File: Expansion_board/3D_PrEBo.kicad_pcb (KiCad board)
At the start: 2 copper layers, 100 x 84 mm, 72 parts, among them J1 LED, J10 TMC_INPUT, J11 Power_out, J12 Z_Probe, J13 Fan_interconnection_header, J14 X_MIN, J15 Z_MAX, J2 V_IN, J3 RJ45, J4 X, J5 Y, J6 Z, J7 E0, J8 E1, J9 FAN&LED_INPUT, M1 Fan_3pin, M2 Fan_3pin, M3 Fan_3pin, M4 Fan_3pin, M5 Fan_3pin, M6 Fan_3pin, M7 Fan_3pin, M8 Fan_4pin, Q1 AOD4189, Q10 IRLML2502, Q2 IRLML2502, Q3 IRLML2502, Q4 IRLML2502, Q5 IRLML2502, Q6 IRLML2502, Q7 IRLML2502, Q8 IRLML2502, Q9 IRLML2502, U1 L5973D, U2 NCP1117-5.0_SOT223

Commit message: Expansion_board: PCB: Place all parts, routing of voltage regulator
Change horizontal fan connector to vertical.
Pour cooper planes on both sides.
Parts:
- C10, C11, C12, C13, C14, C7, C8, C9, JP1, JP2, Q10, Q2, Q3, Q4, Q5, Q6, Q7, Q8, Q9, R10, R11, R12, R13, R2, R6, R7, R8, R9: moved to B.Cu
- J1: footprint Connector_JST:JST_XH_S02B-XH-A-1_1x02_P2.50mm_Horizontal -> Connector_JST:JST_XH_B02B-XH-A_1x02_P2.50mm_Vertical
- J12: footprint Connector:FanPinHeader_1x04_P2.54mm_Vertical -> Connector_JST:JST_XH_B04B-XH-A_1x04_P2.50mm_Vertical
- M1, M2, M3, M4, M5, M6, M7: footprint Connector:FanPinHeader_1x03_P2.54mm_Vertical -> Connector_JST:JST_XH_S03B-XH-A_1x03_P2.50mm_Horizontal
- M8: footprint Connector:FanPinHeader_1x04_P2.54mm_Vertical -> Connector_JST:JST_XH_S04B-XH-A_1x04_P2.50mm_Horizontal
- moved Q3 301.3 mm to (108.6, 85.7), turned to 90 degrees
- moved R6 291.2 mm to (108.6, 89.5), turned to 180 degrees
- moved C1 288.6 mm to (131.6, 113.4)
- moved RV1 284.3 mm to (137.2, 116.8), turned to 180 degrees
- moved C8 283.1 mm to (111.0, 66.0), turned to 180 degrees
- moved D4 273.9 mm to (116.8, 113.8), turned to 180 degrees
- moved C9 273.3 mm to (123.7, 66.0), turned to 180 degrees
- moved R7 272.0 mm to (121.9, 89.5), turned to 180 degrees
- moved M2 271.9 mm to (127.0, 68.6), turned to 180 degrees
- moved Q1 270.2 mm to (127.5, 122.0)
- moved M3 269.2 mm to (139.7, 68.6), turned to 180 degrees
- moved R4 266.5 mm to (135.3, 111.4), turned to 180 degrees
- moved C3 264.6 mm to (131.6, 115.4)
- moved R10 261.0 mm to (152.4, 89.5), turned to 180 degrees
- moved Q4 259.6 mm to (121.9, 85.7), turned to 90 degrees
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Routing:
- net +12V: track 0.00 -> 147.9 mm
- net Net-(C4-Pad1): track 0.00 -> 49.1 mm
- net Net-(C2-Pad1): track 0.00 -> 35.8 mm
- net Net-(C13-Pad2): track 0.00 -> 32.1 mm
- net Net-(D3-Pad2): track 0.00 -> 29.2 mm
- net GND: track 0.00 -> 28.8 mm
- net Net-(C14-Pad2): track 0.00 -> 26.5 mm
- net Net-(C11-Pad2): track 0.00 -> 26.2 mm
- net +24V: track 0.00 -> 25.3 mm
- net FAN0_PWR: track 0.00 -> 25.2 mm
- net Net-(C12-Pad2): track 0.00 -> 24.3 mm
- net FAN2_PWR: track 0.00 -> 22.9 mm
- net FAN1_PWR: track 0.00 -> 22.8 mm
- net Net-(R5-Pad1): track 0.00 -> 14.8 mm
- net Net-(C1-Pad1): track 0.00 -> 12.1 mm
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- added copper zone on B.Cu, net GND
- added copper zone on F.Cu, net GND

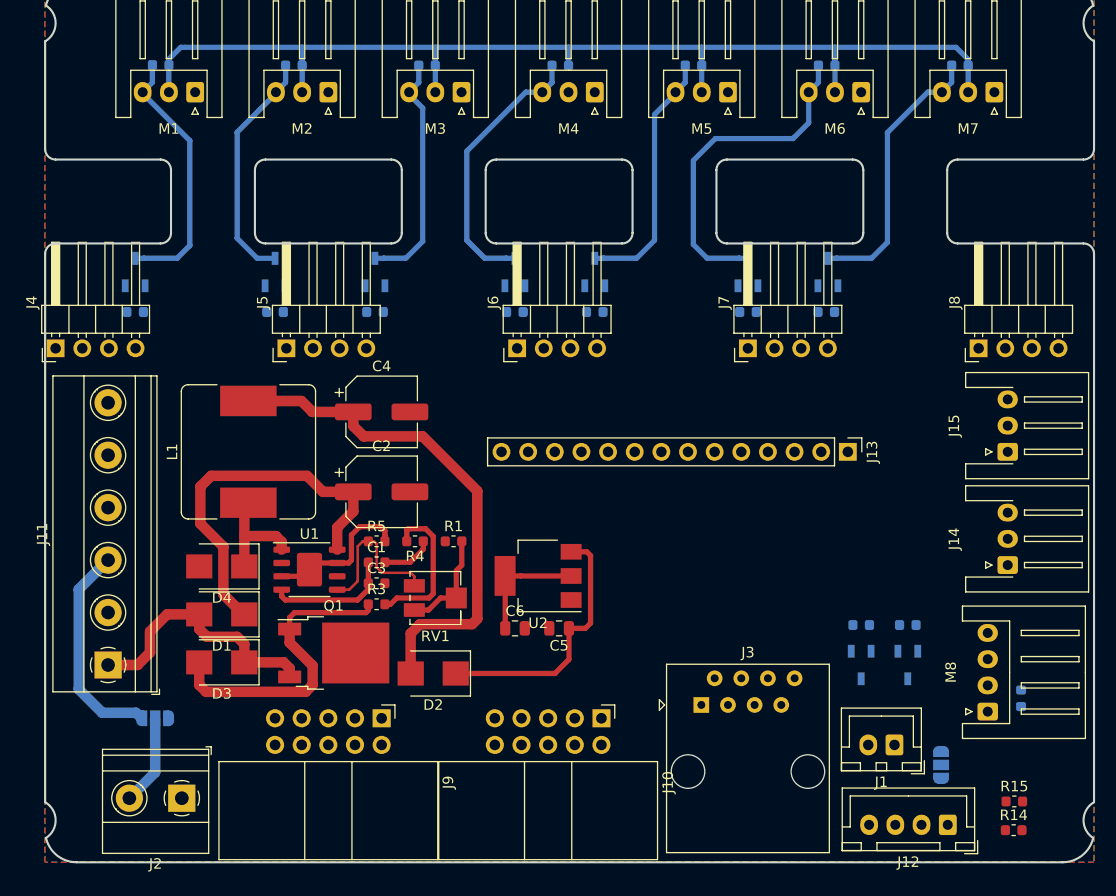
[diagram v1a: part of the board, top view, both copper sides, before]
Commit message: Expansiopn_board: PCB: Routing done, Silk screen in progress
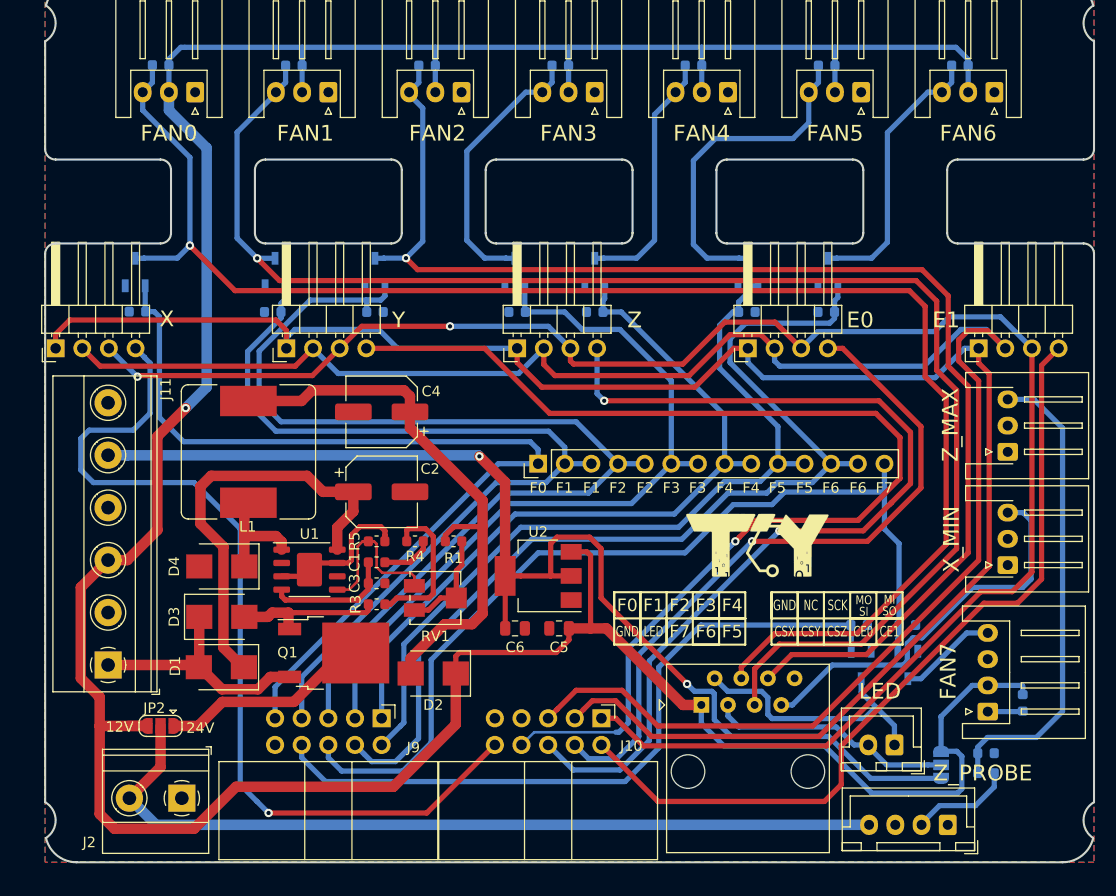
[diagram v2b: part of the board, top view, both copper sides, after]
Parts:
- added G***: LOGO, TCY_logo:TCY_LOGO_13x6mm, F.Cu at (167.9, 111.8)
- JP2: moved to F.Cu
- R14, R15: moved to B.Cu
- moved J13 29.6 mm to (147.0, 104.0), turned to 90 degrees
- moved R14 6.05 mm to (189.7, 133.5)
- moved R15 5.33 mm to (189.7, 131.6), turned to 180 degrees
- moved D1 5.04 mm to (116.8, 123.4)
- moved D3 4.34 mm to (116.8, 118.6), turned to 0 degrees
- moved JP2 0.89 mm to (111.0, 129.0)
- moved C7 0.46 mm to (193.2, 126.8)
- moved R7 0.22 mm to (121.7, 89.5)
- moved R9 0.22 mm to (145.0, 89.5)
- moved R6 0.22 mm to (108.8, 89.5)
- moved R2 0.20 mm to (177.6, 119.4)
- moved R11 0.10 mm to (166.9, 89.5), turned to 0 degrees
- turned C4 to 180 degrees
- turned R8 to 0 degrees
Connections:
- J10 pad 10: CS_E1 -> CS_X
- J10 pad 2: CS_X -> CS_E1
- J10 pad 4: CS_Y -> CS_E0
- J10 pad 8: CS_E0 -> CS_Y
- J12 pad 4: +24V -> V_IN
- J2 pad 2: /V_IN -> V_IN
- J9 pad 1: FAN0 -> FAN4
- J9 pad 2: FAN1 -> FAN5
- J9 pad 3: FAN2 -> FAN3
- J9 pad 4: FAN3 -> FAN6
- J9 pad 5: FAN4 -> FAN2
- J9 pad 6: FAN5 -> FAN7
- J9 pad 7: FAN6 -> FAN1
- J9 pad 8: FAN7 -> LED_IN
- J9 pad 9: LED_IN -> FAN0
- JP2 pad 2: /V_IN -> V_IN
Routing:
- net SCK: track 0.00 -> 176.5 mm
- net MOSI: track 0.00 -> 170.6 mm
- net +12V: track 147.9 -> 318.4 mm, vias 0 -> 1
- net MISO: track 0.00 -> 168.8 mm, vias 0 -> 2
- net FAN0_PWR: track 25.2 -> 146.6 mm, vias 0 -> 1
- net FAN1_PWR: track 22.8 -> 141.1 mm, vias 0 -> 1
- net CS_Y: track 0.00 -> 109.1 mm, vias 0 -> 1
- net FAN2_PWR: track 22.9 -> 125.4 mm, vias 0 -> 1
- net +5V: track 11.3 -> 113.5 mm, vias 0 -> 2
- net FAN2: track 0.00 -> 100.8 mm
- net FAN6: track 0.00 -> 95.1 mm
- net CS_Z: track 0.00 -> 92.2 mm, vias 0 -> 2
- net FAN0: track 0.00 -> 89.2 mm
- net FAN7: track 0.00 -> 89.0 mm
- net CS_X: track 0.00 -> 87.4 mm, vias 0 -> 1
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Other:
- rule trace_min: 0.2 -> 0.25
- board text added: "12V"
- board text added: "24V"
- board text added: "5V"
- board text added: "CE0"
- board text added: "CE1"
- board text added: "CSX"
- board text added: "CSY"
- board text added: "CSZ"
- board text added: "E0"
- board text added: "E1"
- board text added: "F0"
- board text added: "F1"
- board text added: "F2"
- board text added: "F3"
- board text added: "F4"
- board text added: "F5"
- board text added: "F6"
- board text added: "F7"
- board text added: "FAN0"
- board text added: "FAN1"
- board text added: "FAN2"
- board text added: "FAN3"
- board text added: "FAN4"
- board text added: "FAN5"
- board text added: "FAN6"
- board text added: "FAN7"
- board text added: "GND"
- board text added: "LED"
- board text added: "MI"
- board text added: "MO"
- board text added: "NC"
- board text added: "SCK"
- board text added: "SI"
- board text added: "SO"
- board text added: "X"
- board text added: "X_MIN"
- board text added: "Y"
- board text added: "Z"
- board text added: "Z_MAX"
- board text added: "Z_PROBE"

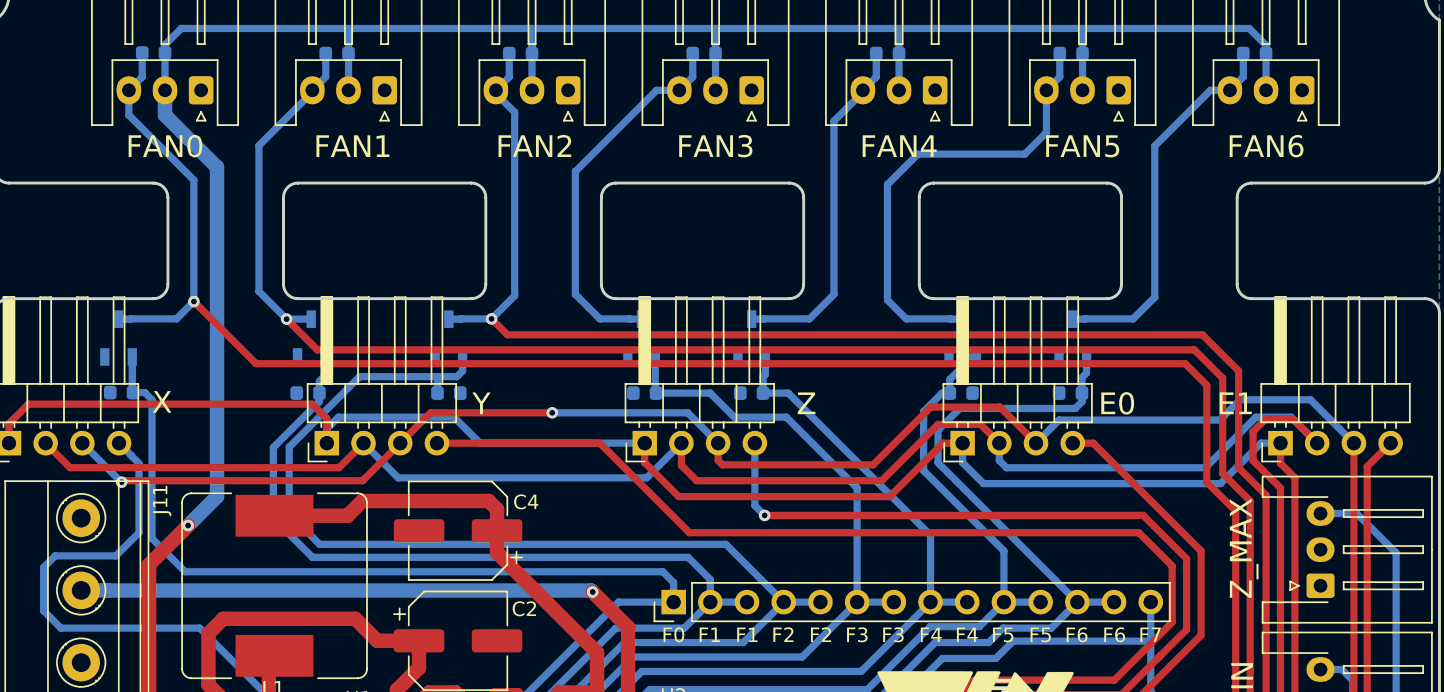
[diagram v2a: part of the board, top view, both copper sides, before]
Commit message: Expansion_board: PCB: Rotate FAN transistors, update bottom silk screen
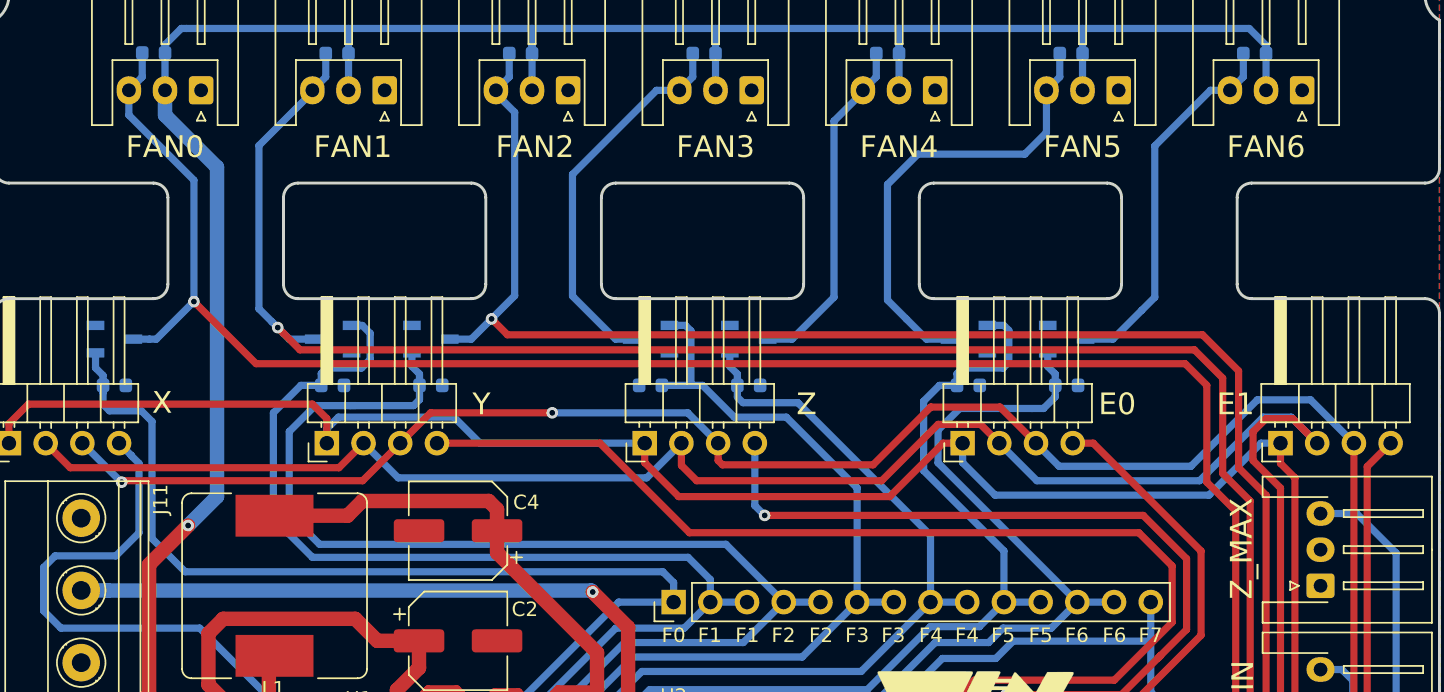
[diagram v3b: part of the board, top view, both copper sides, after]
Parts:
- moved R7 1.78 mm to (123.4, 89.0), turned to 0 degrees
- moved Q4 1.48 mm to (123.4, 85.8), turned to 180 degrees
- moved R8 1.36 mm to (130.2, 89.0)
- moved Q5 1.25 mm to (130.2, 85.8), turned to 0 degrees
- moved R11 0.73 mm to (167.4, 89.0)
- moved R6 0.71 mm to (108.3, 89.0), turned to 0 degrees
- moved R9 0.67 mm to (145.4, 89.0)
- moved Q6 0.62 mm to (145.4, 85.8), turned to 180 degrees
- moved R12 0.60 mm to (174.2, 89.0), turned to 0 degrees
- moved R10 0.57 mm to (152.2, 89.0), turned to 0 degrees
- moved Q9 0.43 mm to (174.2, 85.8), turned to 0 degrees
- moved Q8 0.40 mm to (167.4, 85.8), turned to 180 degrees
- moved Q3 0.29 mm to (108.3, 85.8), turned to 0 degrees
- moved Q7 0.21 mm to (152.2, 85.8), turned to 0 degrees
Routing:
- net FAN1: track 86.2 -> 92.9 mm
- net FAN5: track 77.4 -> 83.3 mm
- net FAN3: track 73.2 -> 75.9 mm
- net FAN0: track 89.2 -> 91.7 mm
- net FAN4: track 72.1 -> 74.5 mm
- net FAN1_PWR: track 141.1 -> 142.9 mm
- net FAN6: track 95.1 -> 93.4 mm
- net FAN2: track 100.8 -> 99.3 mm
- net MISO: track 168.8 -> 170.1 mm
- net MOSI: track 170.6 -> 171.3 mm
- net FAN2_PWR: track 125.4 -> 125.9 mm
